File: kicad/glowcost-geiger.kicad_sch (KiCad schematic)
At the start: 75 parts, among them J1 JST GH 4-pin, J2 C142864 DNP, J3 C142864 DNP, Q1 MMBT3904LT1G, Q2 MMBT3904LT1G, U1 UNIMPLEMENTED HV, U2 UNIMPLEMENTED LOGIC

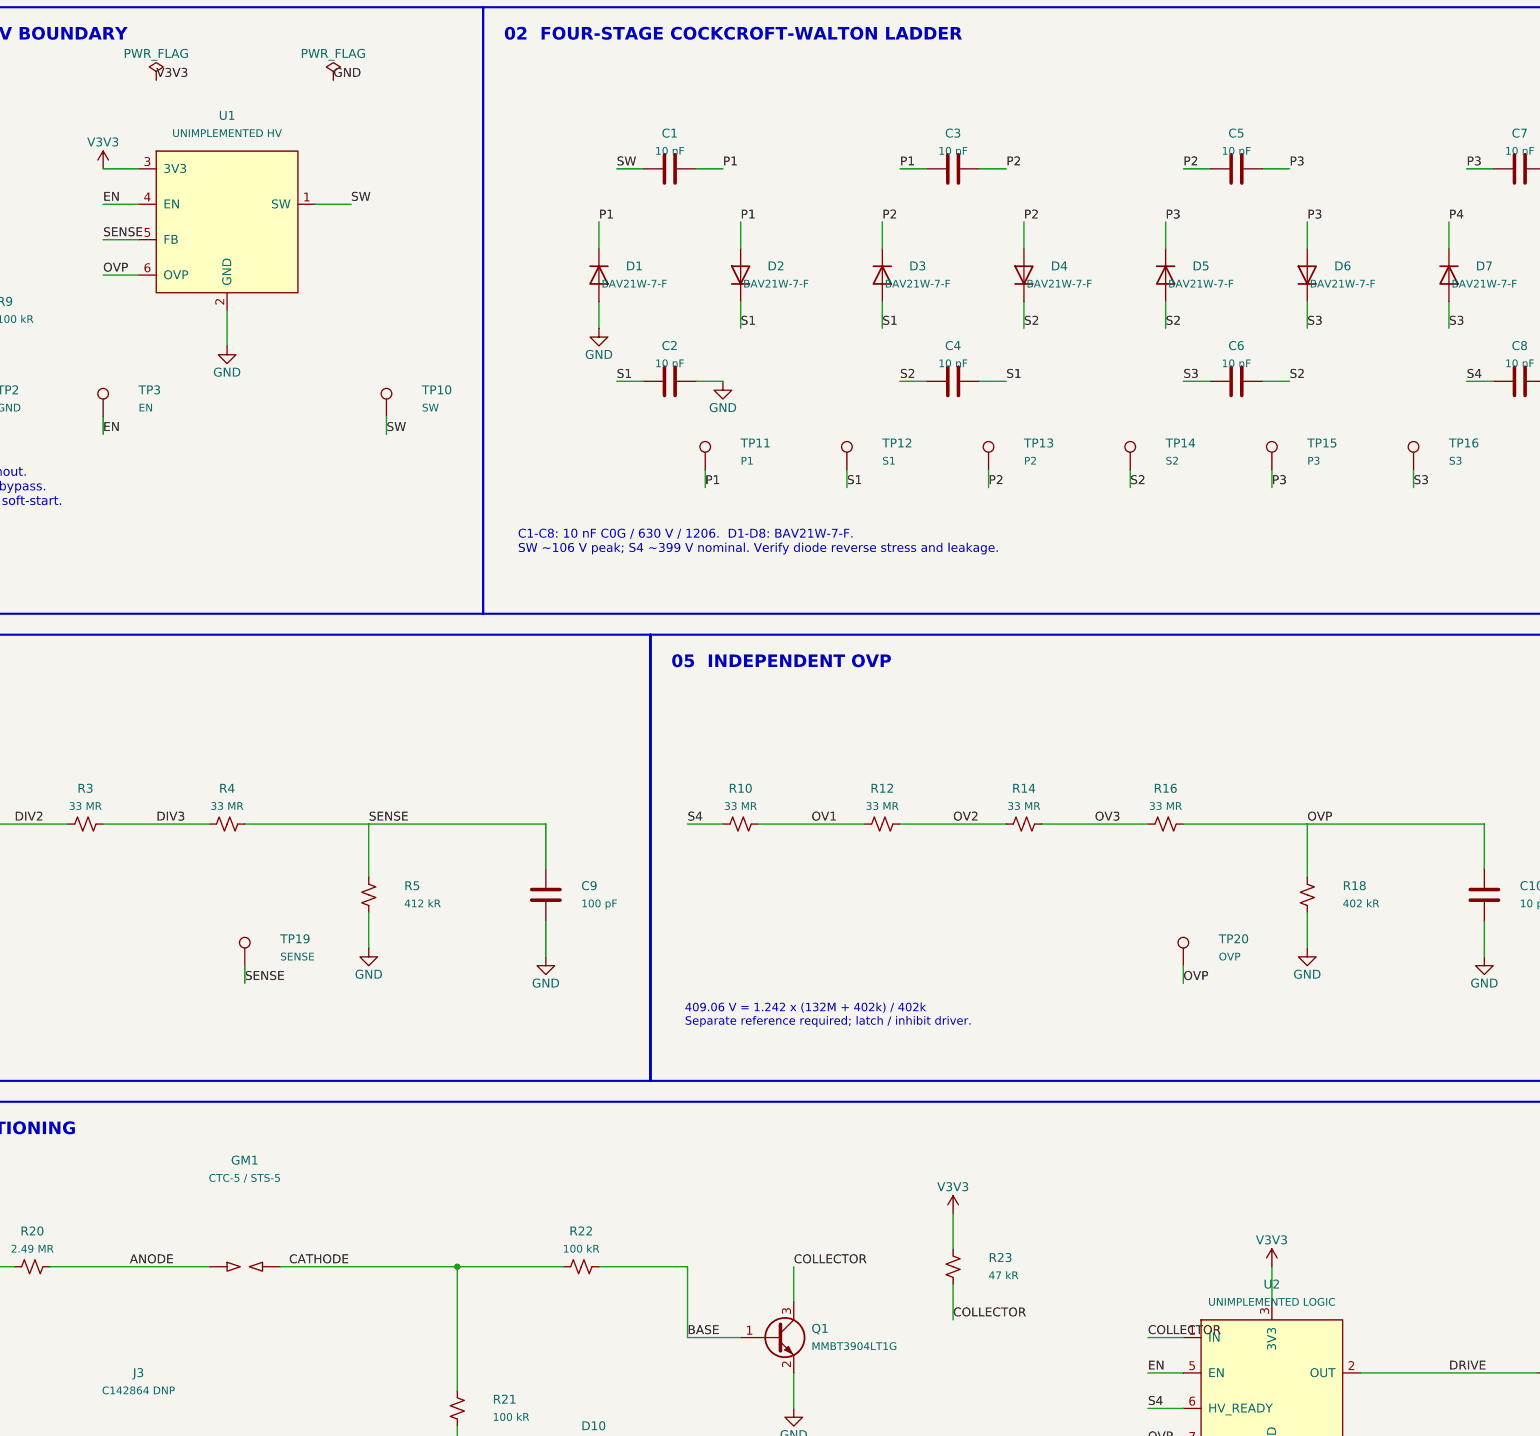
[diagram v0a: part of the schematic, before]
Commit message: Replace behavioral parts and remove tscircuit workflow
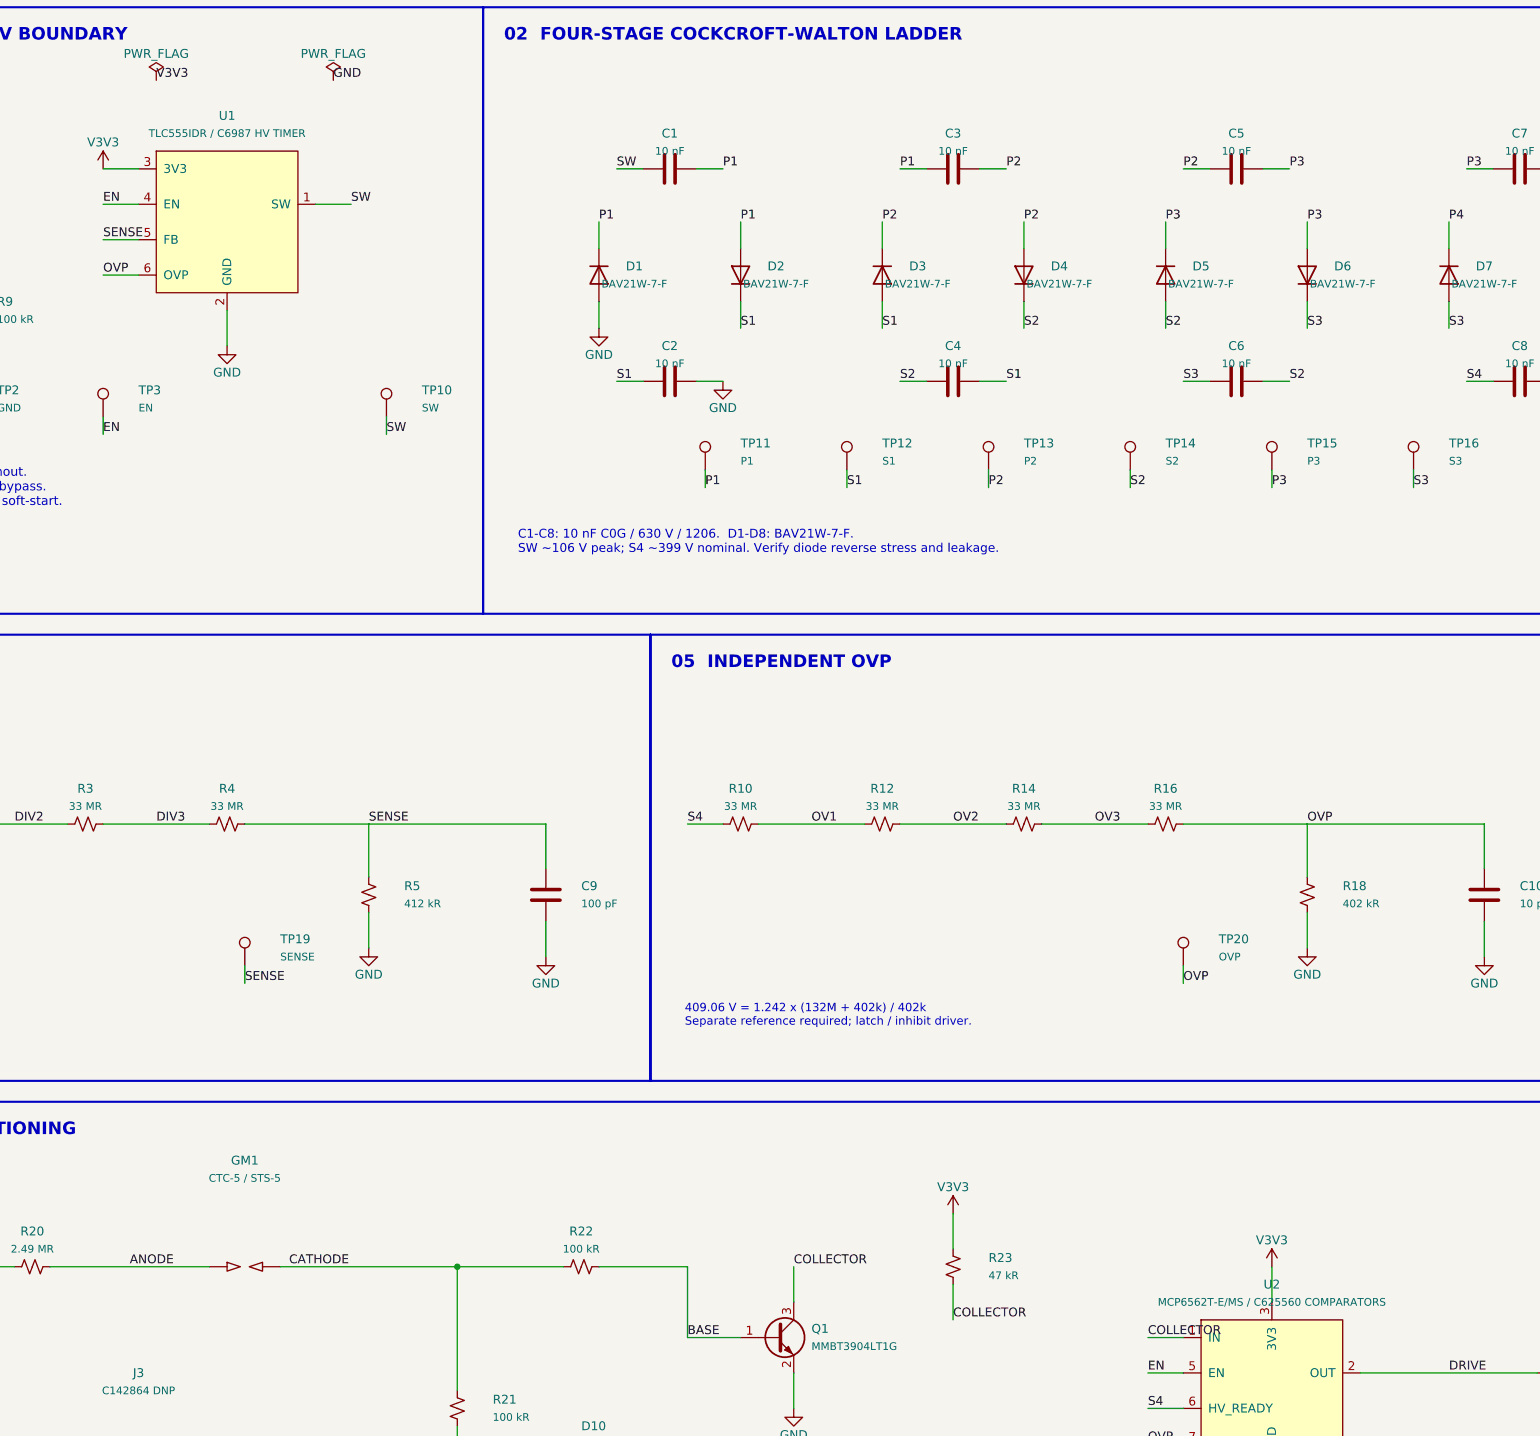
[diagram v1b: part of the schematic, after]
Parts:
- U1: value UNIMPLEMENTED HV -> TLC555IDR / C6987 HV TIMER
- U2: value UNIMPLEMENTED LOGIC -> MCP6562T-E/MS / C625560 COMPARATORS

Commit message: Add ATtiny1616-only schematic and STEMMA/boost block
Replace U1/U2 behavioral boundaries with ATtiny1616-MNR PWM HV drive,
dual STEMMA QT, and boost FET/inductor. Sync pin map, handoff docs, and
firmware pin headers.
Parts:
- removed U1: TLC555IDR / C6987 HV TIMER, symbol Glowcost:Analog_HV_boundary
- removed U2: MCP6562T-E/MS / C625560 COMPARATORS, symbol Glowcost:Pulse_logic_boundary
- added C11: 100 nF, glowcost:C1, symbol Glowcost:C
- added J4, J5: SM04B-SRSS-TB / C160404, glowcost:J1, symbol Glowcost:Conn_01x04
- added JP2: A0 open=high, glowcost:SJ_LED, symbol Glowcost:SolderJumper_2_Bridged
- added JP3: A1 open=high, glowcost:SJ_LED, symbol Glowcost:SolderJumper_2_Bridged
- added L1: 1 mH B82442T1105K050, Inductor_SMD:L_1210_3225Metric, symbol Glowcost:L
- added Q3: HL2310A / C7420347, Package_TO_SOT_SMD:SOT-23, symbol Glowcost:HL2310A
- added R25: 220 R, glowcost:R1, symbol Glowcost:R_Small_US
- added R26, R27: 4.7 kR, glowcost:R1, symbol Glowcost:R_Small_US
- added R28, R29: 10 kR, glowcost:R1, symbol Glowcost:R_Small_US
- added TP23: V3V3, glowcost:TP1, symbol Glowcost:TestPoint
- added TP24: UPDI, glowcost:TP1, symbol Glowcost:TestPoint
- added TP25, TP29: GND, glowcost:TP1, symbol Glowcost:TestPoint
- added TP28: UART_TX, glowcost:TP1, symbol Glowcost:TestPoint
- added U1: ATTINY1616-MNR / C507118, Package_DFN_QFN:VQFN-20-1EP_3x3mm_P0.4mm_EP1.7x1.7mm, symbol Glowcost:ATtiny1616-M
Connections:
- net ANODE: no longer TP21.1
- net BASE: no longer TP6.1
- net CATHODE: no longer TP8.1
- net COLLECTOR: now also R24.1, R7.1, U1.1 (PA2); no longer TP7.1
- net EN: now also U1.11 (PB3); no longer TP3.1
- net GND: now also C11.2, J4.1 (Pin_1), J5.1 (Pin_1), JP2.2 (B), JP3.2 (B), Q3.2 (S), R29.2, TP25.1, TP29.1, U1.21 (GND), U1.3 (GND); no longer TP2.1, TP22.1, TP9.1
- net OVP: no longer TP20.1
- net P1: no longer TP11.1
- net P2: no longer TP13.1
- net P3: no longer TP15.1
- net P4: no longer TP17.1
- net S1: no longer TP12.1
- net S2: no longer TP14.1
- net S3: no longer TP16.1
- net S4: no longer TP18.1
- net SENSE: now also U1.7 (PA6); no longer TP19.1
- net SW: now also L1.2, Q3.3 (D); no longer TP10.1
- net TTL: no longer TP4.1
- net V3V3: now also C11.1, J4.2 (Pin_2), J5.2 (Pin_2), L1.1, R26.1, R27.1, R28.1, TP23.1, U1.4 (VCC); no longer TP1.1
- removed net DRIVE: R24.1, R7.1, TP5.1
- new net A0: JP2.1 (A), U1.14 (PB0)
- new net A1: JP3.1 (A), U1.13 (PB1)
- new net GATE: Q3.1 (G), R25.2
- new net HV_PWM: R25.1, U1.12 (PB2)
- new net SCL: J4.4 (Pin_4), J5.4 (Pin_4), R27.2, U1.6 (PA5)
- new net SDA: J4.3 (Pin_3), J5.3 (Pin_3), R26.2, U1.5 (PA4)
- new net UART_TX: TP28.1, U1.20 (PA1)
- new net UPDI: TP24.1, U1.19 (~{RESET}/PA0)
- new net V3V3_SENSE: R28.2, R29.1, U1.8 (PA7)
- no-connect marks 0 -> 7
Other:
- note added: "ATtiny-only: PWM boost + pulse/I2C/ADC. USART0 alt TX=PA1 (PB2=HV_PWM). I2C default 0x2F."
- note added: "Boost (was U1 black-box)"
- note added: "DRIVE merged into COLLECTOR. No TLC555/MCP6562."
- note added: "JP2/JP3: leave OPEN for 0x2F; bridge to GND for low"
- note added: "Q3: 1=G 2=S 3=D; R25 gate. L1 DCR 9.5R — efficiency risk."
- note added: "STEMMA QT JST SH 1=GND 2=V+ 3=SDA 4=SCL"
- note added: "U1: PA2=COLLECTOR PA4=SDA PA5=SCL PA6=SENSE PA7=V3V3_SENSE | PB0=A0 PB1=A1 PB2=HV_PWM PB3=EN PA0=UPDI PA1=UART_TX"
- note added: "UPDI / UART pads"

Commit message: Tidy ATtiny schematic ERC and refresh jev report
Wire probe TP/power-flag nets, re-anchor boost/decap labels, clear all
ERC errors. Jev deterministic gate refreshed (API key not available).
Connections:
- net ANODE: now also TP21.1
- net BASE: now also TP6.1
- net CATHODE: now also TP8.1
- net COLLECTOR: now also TP5.1, TP7.1
- net EN: now also TP3.1
- net GND: now also TP2.1, TP22.1, TP9.1
- net OVP: now also TP20.1
- net P1: now also TP11.1
- net P2: now also TP13.1
- net P3: now also TP15.1
- net P4: now also TP17.1
- net S1: now also TP12.1
- net S2: now also TP14.1
- net S3: now also TP16.1
- net S4: now also TP18.1
- net SENSE: now also TP19.1
- net SW: now also TP10.1
- net TTL: now also TP4.1
- net V3V3: now also TP1.1

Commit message: Apply Jev schematic layout winners and add decision helper
Cluster probes on an edge strip, annotate left-to-right block frames,
keep label-based long nets. Add jev_schematic_review helper/report;
refresh PCB jev answers. ERC errors remain 0; core nets unchanged.
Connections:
- net OVP: no longer C10.1, R16.2, R18.1
- new net: C10.1, R16.2, R18.1
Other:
- note added: "HV / TUBE / PULSE"
- note added: "MCU + BOOST"
- note added: "PI HEADER"
- note added: "PROBE STRIP"
- note added: "STEMMA / I2C"
- moved on the sheet: TP1, TP10, TP11, TP12, TP13, TP14, TP15, TP16, TP17, TP18, TP19, TP2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

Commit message: Polish ATtiny schematic layout and clear overlaps
Boost/STEMMA placement, probe strip pitch, hide noisy fields; ERC 0 and core nets intact.
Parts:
- removed TP11: P1, glowcost:TP11, symbol Glowcost:TestPoint
- removed TP12: S1, glowcost:TP12, symbol Glowcost:TestPoint
- removed TP13: P2, glowcost:TP13, symbol Glowcost:TestPoint
- removed TP14: S2, glowcost:TP14, symbol Glowcost:TestPoint
- removed TP15: P3, glowcost:TP15, symbol Glowcost:TestPoint
- removed TP16: S3, glowcost:TP16, symbol Glowcost:TestPoint
- removed TP17: P4, glowcost:TP17, symbol Glowcost:TestPoint
- removed TP18: S4, glowcost:TP18, symbol Glowcost:TestPoint
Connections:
- net ANODE: no longer GM1.1, R20.2
- net CATHODE: no longer GM1.2, R21.1, R22.1
- net ANODE_MID: no longer names the net of R19.2, R20.1
- net BL1: no longer names the net of R11.2, R13.1
- net BL2: no longer names the net of R13.2, R15.1
- net BL3: no longer names the net of R15.2, R17.1
- net DIV1: no longer names the net of R1.2, R2.1
- net DIV2: no longer names the net of R2.2, R3.1
- net DIV3: no longer names the net of R3.2, R4.1
- net LED_A: no longer names the net of D9.1 (A), R6.2
- net LED_BASE: no longer names the net of Q2.1 (B), R7.2, R8.1
- net LED_SUPPLY: no longer names the net of JP1.2 (B), R6.1
- net OV1: no longer names the net of R10.2, R12.1
- net OV2: no longer names the net of R12.2, R14.1
- net OV3: no longer names the net of R14.2, R16.1
- new net: GM1.1, R20.2
- new net: GM1.2, R21.1, R22.1
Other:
- note added: "ATtiny-only: MCU PWM boost + pulse/I2C/ADC. No 555/MCP6562. Dual STEMMA J4/J5."
- note added: "BOOST"
- note added: "C1-C8: 10nF C0G 630V 1206. D1-D8: BAV21W-7-F. SW~106Vpk; S4~399V nom."
- note added: "CTRL"
- note added: "HV"
- note added: "HV LADDER"
- note added: "HV MULTIPLIER"
- note added: "Independent OVP divider; verify diode reverse stress/leakage."
- note added: "MCU"
- note added: "NOTES"
- note added: "OVP"
- note added: "OVP / PULSE"
- note added: "PA2=COLLECTOR PA4=SDA PA5=SCL PA6=SENSE PA7=V3V3_SENSE"
- note added: "PB0=A0 PB1=A1 PB2=HV_PWM PB3=EN PA0=UPDI PA1=UART_TX (USART0 alt)"
- note added: "PI"
- note added: "PI J1: 1=3V3 2=GND 3=PULSE 4=EN"
- note added: "PIN MAP (U1)"
- note added: "PROBES"
- note added: "PROG"
- note added: "PWR"
- note added: "Q3 HL2310A (1=G 2=S 3=D); R25 gate; L1 1mH DCR 9.5R (efficiency risk)."
- note removed: "01 PI INPUT + ANALOG HV BOUNDARY"
- note removed: "02 FOUR-STAGE COCKCROFT-WALTON LADDER"
- note removed: "03 GREEN 0805 PULSE INDICATOR"
- note removed: "04 MAIN HV FEEDBACK"
- note removed: "05 INDEPENDENT OVP"
- note removed: "06 PASSIVE HV DISCHARGE"
- note removed: "07 TUBE + PULSE CONDITIONING"
- note removed: "40 MR total: 10 uA, 4 mW at 400 V. Always connected; EN low does not prove discharge. Model: ~158 V remains at 100 ms after disable."
- note removed: "409.06 V = 1.242 x (132M + 402k) / 402k Separate reference required; latch / inhibit driver."
- note removed: "ATtiny-only: PWM boost + pulse/I2C/ADC. USART0 alt TX=PA1 (PB2=HV_PWM). I2C default 0x2F."
- note removed: "Boost (was U1 black-box)"
- note removed: "C1-C8: 10 nF C0G / 630 V / 1206. D1-D8: BAV21W-7-F. SW ~106 V peak; S4 ~399 V nominal. Verify diode reverse stress and leakage."
- note removed: "GLOWCOST GEIGER | 3.3 V | CTC-5 | COUNTS-FIRST MONITOR"
- note removed: "J1: 1=3V3 2=GND 3=PULSE 4=EN U1 is a functional boundary, not an IC pinout. 1 mH; 10 kHz; 20 us ON; 22 uF modeled bypass. Implement oscillator / driver / feedback / soft-start."
- note removed: "MCU + BOOST"
- note removed: "PROTOTYPE / HV SAFETY NOTES"
- note removed: "Q3: 1=G 2=S 3=D; R25 gate. L1 DCR 9.5R — efficiency risk."
- note removed: "U1: PA2=COLLECTOR PA4=SDA PA5=SCL PA6=SENSE PA7=V3V3_SENSE | PB0=A0 PB1=A1 PB2=HV_PWM PB3=EN PA0=UPDI PA1=UART_TX"
- moved on the sheet: C11, J4, J5, JP2, JP3, L1, Q3, R25, R26, R27, R28, R29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
